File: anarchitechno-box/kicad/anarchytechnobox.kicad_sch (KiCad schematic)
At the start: 27 parts, among them J3 Screw_Terminal_01x03, J4 Screw_Terminal_01x03, J5 Screw_Terminal_01x03, J6 Screw_Terminal_01x03, M1 Fan_Tacho_PWM

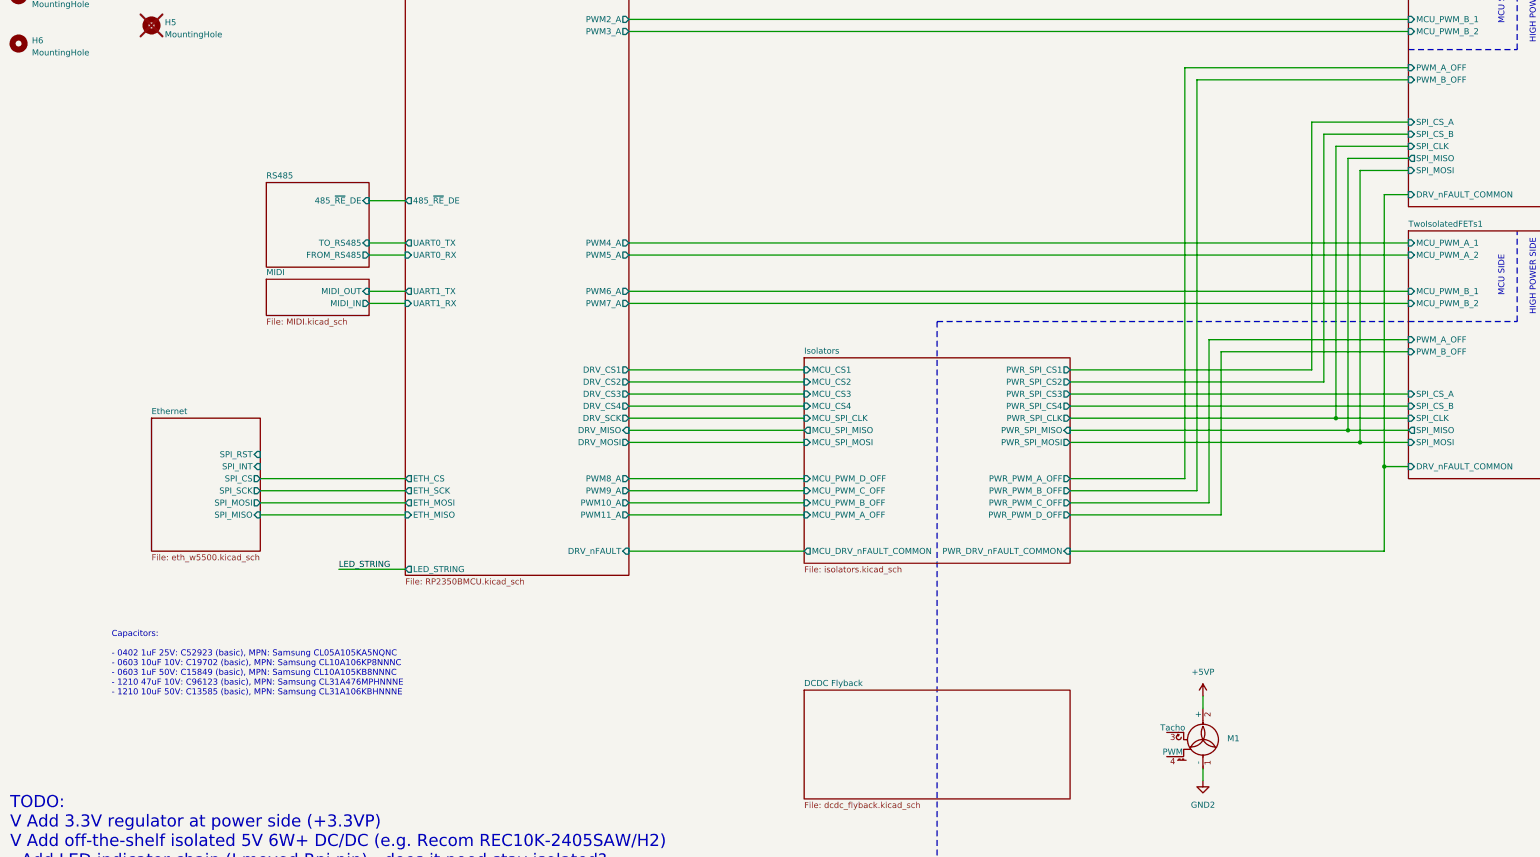
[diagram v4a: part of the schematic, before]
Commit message: - Logo Robot Theater lab - UART connector - RF antenne clearance aangepast - Reset/interrupt pins ethernet aangesloten
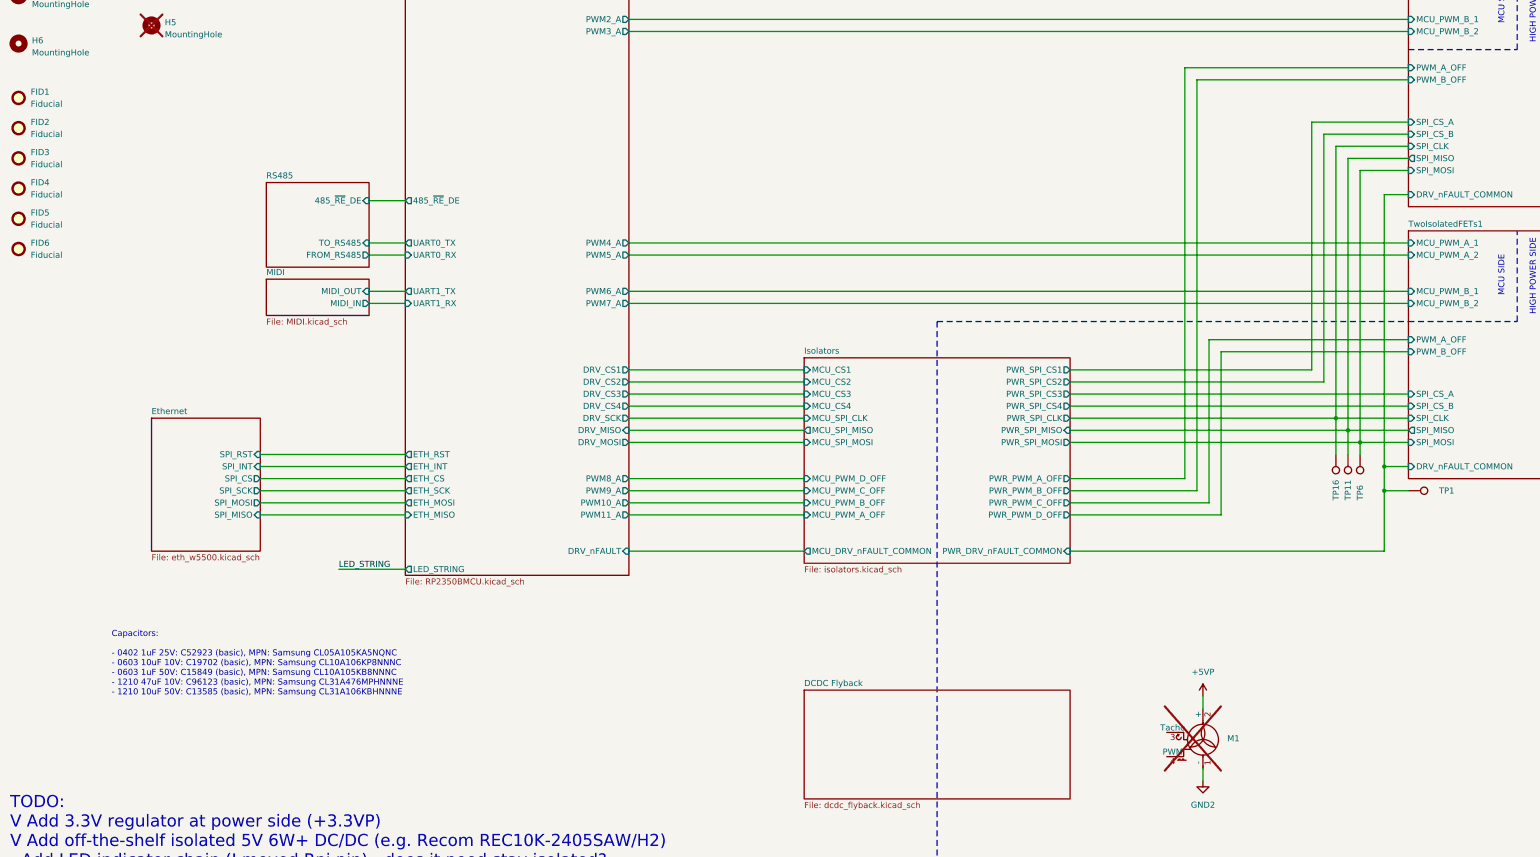
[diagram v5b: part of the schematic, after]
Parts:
- added FID1, FID2, FID3, FID4, FID5, FID6: Fiducial, Fiducial:Fiducial_1mm_Mask2mm, symbol Mechanical:Fiducial
- added TP1, TP11, TP16, TP6: TestPoint, TestPoint:TestPoint_Pad_D1.0mm, symbol Connector:TestPoint
- M1: now not fitted; now left out of the parts list
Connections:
- net Isolators/PWR_DRV_nFAULT_COMMON: now also TP1.1
- net Isolators/PWR_SPI_CLK: now also TP16.1
- net Isolators/PWR_SPI_MISO: now also TP11.1
- net Isolators/PWR_SPI_MOSI: now also TP6.1
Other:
- sheet RP2350BMCU ports: added ETH_INT, ETH_RST; removed none

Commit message: BOM nagelopen, bestelklaar.
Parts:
- D18, D19, D2, D20, D21, D22, D23, D3: value C5349953 -> XL-1010RGBC-2812B; LCSC Part (none) -> C5349953
- H1, H3, H4, H6, TP1, TP11, TP16, TP6: now left out of the parts list
- J3, J4, J5, J6: LCSC Part (none) -> C2827883
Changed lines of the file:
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@@
 			)
 		)
-		(property "Value" "C5349953"
+		(property "Value" "XL-1010RGBC-2812B"
 			(at 440.69 -19.05 0)
 			(effects
@@
 			)
 		)
+		(property "LCSC Part" "C5349953"
+			(at 440.69 -19.05 0)
+			(effects
+				(font
+					(size 1.27 1.27)
+				)
+				(hide yes)
+			)
+		)
 		(pin "1"
 		)
@@
 			)
 		)
-		(property "Value" "C5349953"
+		(property "Value" "XL-1010RGBC-2812B"
 			(at 394.97 -19.05 0)
 			(effects
@@
 			)
 		)
+		(property "LCSC Part" "C5349953"
+			(at 394.97 -19.05 0)
+			(effects
+				(font
+					(size 1.27 1.27)
+				)
+				(hide yes)
+			)
+		)
 		(pin "1"
 		)
@@
 			)
 		)
-		(property "Value" "C5349953"
+		(property "Value" "XL-1010RGBC-2812B"
 			(at 326.39 -19.05 0)
 			(effects
@@
 			)
 		)
+		(property "LCSC Part" "C5349953"
+			(at 326.39 -19.05 0)
+			(effects
+				(font
+					(size 1.27 1.27)
+				)
+				(hide yes)
+			)
+		)
 		(pin "1"
 		)
@@
 			)
 		)
-		(property "Value" "C5349953"
+		(property "Value" "XL-1010RGBC-2812B"
 			(at 280.67 -19.05 0)
 			(effects
@@
 			)
 		)
+		(property "LCSC Part" "C5349953"
+			(at 280.67 -19.05 0)
+			(effects
+				(font
+					(size 1.27 1.27)
+				)
+				(hide yes)
+			)
+		)
 		(pin "1"
 		)
@@
 		(unit 1)
 		(exclude_from_sim no)
-		(in_bom yes)
+		(in_bom no)
 		(on_board yes)
 		(dnp no)
@@
 			)
 		)
-		(property "Value" "C5349953"
+		(property "Value" "XL-1010RGBC-2812B"
 			(at 372.11 -19.05 0)
 			(effects
@@
 			)
 		)
+		(property "LCSC Part" "C5349953"
+			(at 372.11 -19.05 0)
+			(effects
+				(font
+					(size 1.27 1.27)
+				)
+				(hide yes)
+			)
+		)
 		(pin "1"
 		)
@@
 		(unit 1)
 		(exclude_from_sim no)
-		(in_bom yes)
+		(in_bom no)
 		(on_board yes)
 		(dnp no)
@@
 		(unit 1)
 		(exclude_from_sim no)
-		(in_bom yes)
+		(in_bom no)
 		(on_board yes)
 		(dnp no)
@@
 			)
 		)
-		(property "Value" "C5349953"
+		(property "Value" "XL-1010RGBC-2812B"
 			(at 349.25 -19.05 0)
 			(effects
@@
 			)
 		)
+		(property "LCSC Part" "C5349953"
+			(at 349.25 -19.05 0)
+			(effects
+				(font
+					(size 1.27 1.27)
+				)
+				(hide yes)
+			)
+		)
 		(pin "1"
 		)
@@
 			)
 		)
+		(property "LCSC Part" "C2827883"
+			(at 382.27 39.37 0)
+			(effects
+				(font
+					(size 1.27 1.27)
+				)
+				(hide yes)
+			)
+		)
 		(pin "1"
 		)
@@
 			)
 		)
+		(property "LCSC Part" "C2827883"
+			(at 382.27 86.36 0)
+			(effects
+				(font
+					(size 1.27 1.27)
+				)
+				(hide yes)
+			)
+		)
 		(pin "1"
 		)
@@
 		(unit 1)
 		(exclude_from_sim no)
-		(in_bom yes)
+		(in_bom no)
 		(on_board yes)
 		(dnp no)
@@
 		(unit 1)
 		(exclude_from_sim no)
-		(in_bom yes)
+		(in_bom no)
 		(on_board yes)
 		(dnp no)
@@
 		(unit 1)
 		(exclude_from_sim no)
-		(in_bom yes)
+		(in_bom no)
 		(on_board yes)
 		(dnp no)
@@
 			)
 		)
-		(property "Value" "C5349953"
+		(property "Value" "XL-1010RGBC-2812B"
 			(at 303.53 -19.05 0)
 			(effects
@@
 			)
 		)
+		(property "LCSC Part" "C5349953"
+			(at 303.53 -19.05 0)
+			(effects
+				(font
+					(size 1.27 1.27)
+				)
+				(hide yes)
+			)
+		)
 		(pin "1"
 		)
@@
 			)
 		)
+		(property "LCSC Part" "C2827883"
+			(at 382.27 96.52 0)
+			(effects
+				(font
+					(size 1.27 1.27)
+				)
+				(hide yes)
+			)
+		)
 		(pin "1"
 		)
@@
 			)
 		)
+		(property "LCSC Part" "C2827883"
+			(at 382.27 29.21 0)
+			(effects
+				(font
+					(size 1.27 1.27)
+				)
+				(hide yes)
+			)
+		)
 		(pin "1"
 		)
@@
 			)
 		)
-		(property "Value" "C5349953"
+		(property "Value" "XL-1010RGBC-2812B"
 			(at 417.83 -19.05 0)
 			(effects
@@
 			)
 		)
+		(property "LCSC Part" "C5349953"
+			(at 417.83 -19.05 0)
+			(effects
+				(font
+					(size 1.27 1.27)
+				)
+				(hide yes)
+			)
+		)
 		(pin "1"
 		)
@@
 		(unit 1)
 		(exclude_from_sim no)
-		(in_bom yes)
+		(in_bom no)
 		(on_board yes)
 		(dnp no)
@@
 		(unit 1)
 		(exclude_from_sim no)
-		(in_bom yes)
+		(in_bom no)
 		(on_board yes)
 		(dnp no)
